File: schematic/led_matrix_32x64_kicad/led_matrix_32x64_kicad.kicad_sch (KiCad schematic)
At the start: 3 parts, among them J1 Conn_02x08_Odd_Even, SW1 SW_Push, U1 Pico

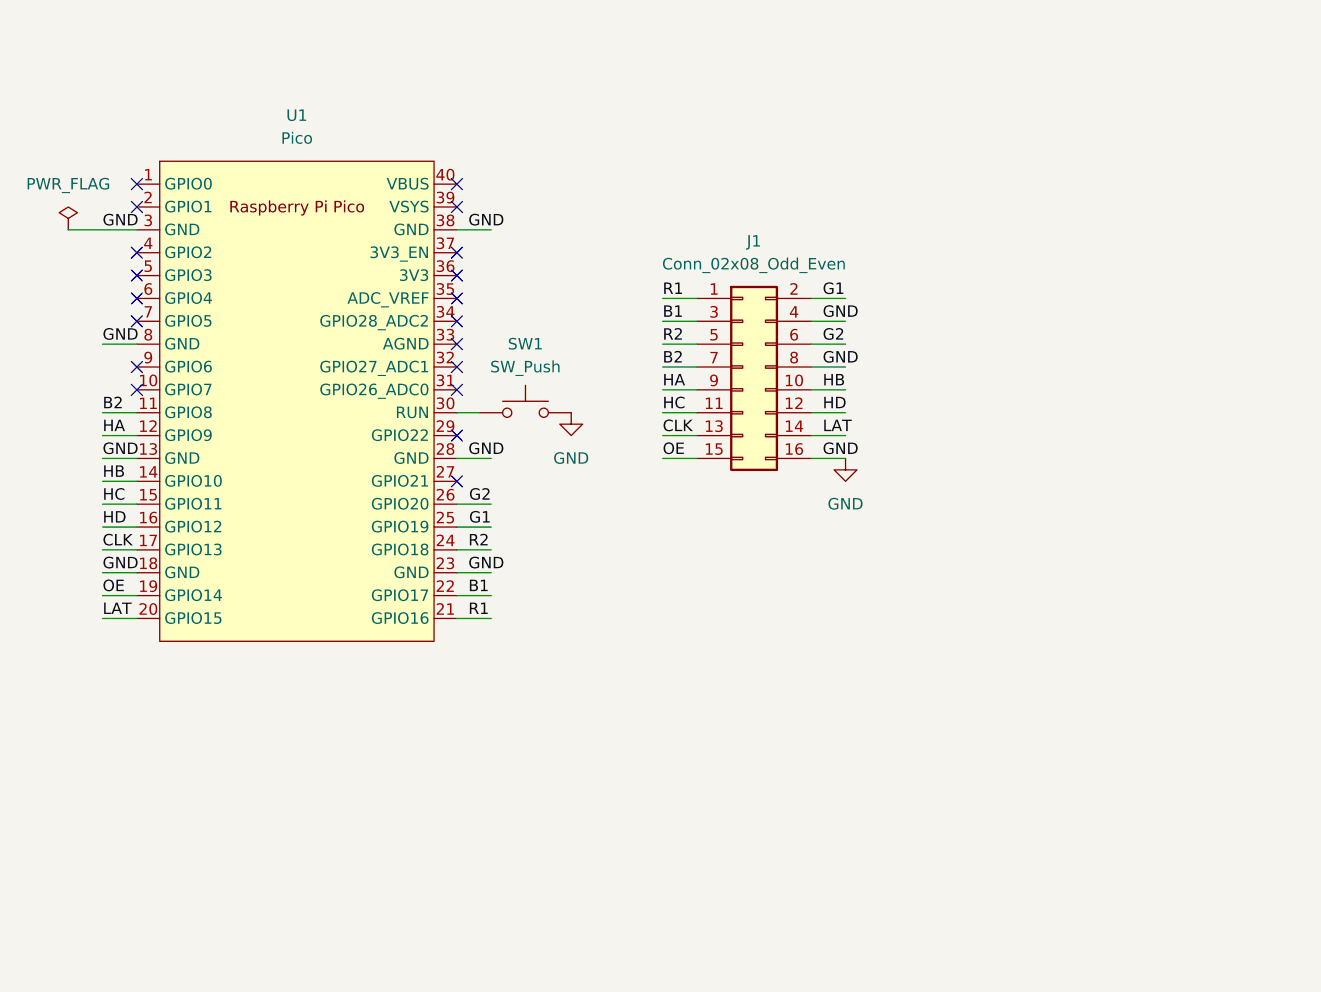
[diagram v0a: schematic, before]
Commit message: Starting the 32x64 matrix with a copy of the 8x8 dotstar.
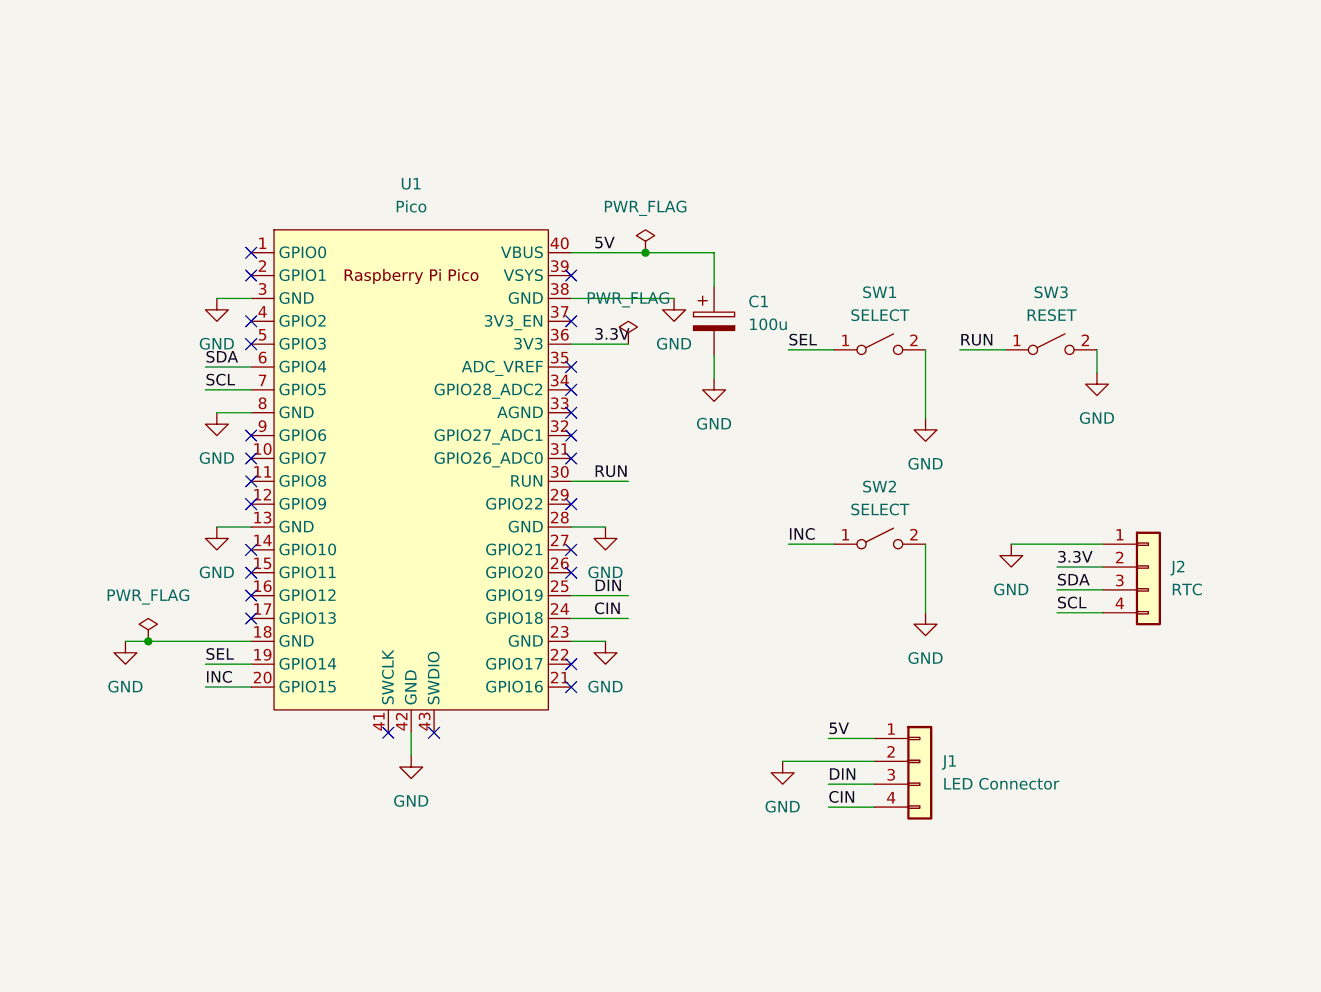
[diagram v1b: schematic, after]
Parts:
- removed J1: Conn_02x08_Odd_Even, Connector_PinHeader_2.54mm:PinHeader_2x08_P2.54mm_Vertical, symbol Connector_Generic:Conn_02x08_Odd_Even
- removed SW1: SW_Push, Button_Switch_THT:SW_PUSH_6mm, symbol Switch:SW_Push
- removed U1: Pico, Raspberry_Pi_Pico:RPi_Pico_SMD_TH, symbol PI PICO:Pico
- added C1: 100u, Capacitor_THT:CP_Radial_D6.3mm_P2.50mm, symbol Device:C_Polarized
- added J1: LED Connector, Connector_PinHeader_2.54mm:PinHeader_1x04_P2.54mm_Vertical, symbol Connector_Generic:Conn_01x04
- added J2: RTC, Connector_PinHeader_2.54mm:PinHeader_1x04_P2.54mm_Vertical, symbol Connector_Generic:Conn_01x04
- added SW1, SW2: SELECT, Button_Switch_THT:SW_PUSH-12mm, symbol Switch:SW_SPST
- added SW3: RESET, Matt:SMD_Button_6mm_3_5mm, symbol Switch:SW_SPST
- added U1: Pico, Raspberry_Pi_Pico:RPi_Pico_SMD_TH, symbol PI Pico:Pico
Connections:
- net GND: now also C1.2, J1.2 (Pin_2), J2.1 (Pin_1), SW1.2 (B), SW2.2 (B), SW3.2 (B), U1.13 (GND), U1.18 (GND), U1.23 (GND), U1.28 (GND), U1.3 (GND), U1.38 (GND), U1.42 (GND), U1.8 (GND)
- new net 3.3V: J2.2 (Pin_2), U1.36 (3V3)
- new net 5V: C1.1, J1.1 (Pin_1), U1.40 (VBUS)
- new net CIN: J1.4 (Pin_4), U1.24 (GPIO18)
- new net DIN: J1.3 (Pin_3), U1.25 (GPIO19)
- new net INC: SW2.1 (A), U1.20 (GPIO15)
- new net RUN: SW3.1 (A), U1.30 (RUN)
- new net SCL: J2.4 (Pin_4), U1.7 (GPIO5)
- new net SDA: J2.3 (Pin_3), U1.6 (GPIO4)
- new net SEL: SW1.1 (A), U1.19 (GPIO14)
- no-connect marks 19 -> 26
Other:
- title: PI Pico to 32x64 LED Matrix interface board -> Matrix Clock

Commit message: Mapped 32x64 pins to PICO
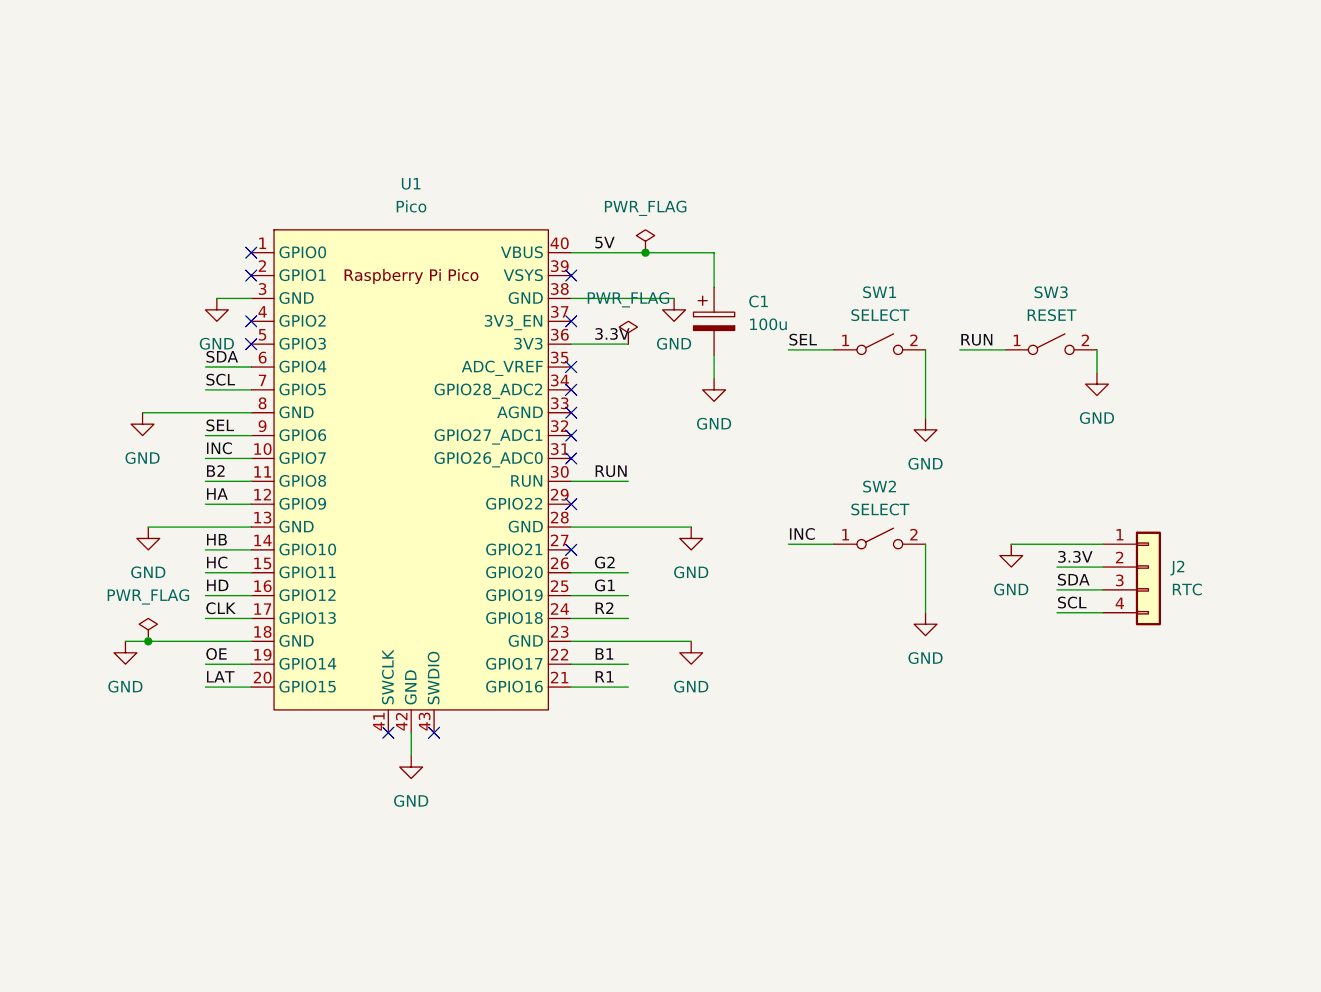
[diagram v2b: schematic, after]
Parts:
- removed J1: LED Connector, Connector_PinHeader_2.54mm:PinHeader_1x04_P2.54mm_Vertical, symbol Connector_Generic:Conn_01x04
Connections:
- net INC: now also U1.10 (GPIO7); no longer U1.20 (GPIO15)
- net SEL: now also U1.9 (GPIO6); no longer U1.19 (GPIO14)
- net B2: now reaches U1.11 (GPIO8)
- net HA: now reaches U1.12 (GPIO9)
- net HB: now reaches U1.14 (GPIO10)
- net HC: now reaches U1.15 (GPIO11)
- net HD: now reaches U1.16 (GPIO12)
- net CLK: now reaches U1.17 (GPIO13)
- net R1: now reaches U1.21 (GPIO16)
- net B1: now reaches U1.22 (GPIO17)
- net G2: now reaches U1.26 (GPIO20)
- net CIN renamed R2
- net DIN renamed G1
- new net LAT: U1.20 (GPIO15)
- new net OE: U1.19 (GPIO14)
- no-connect marks 26 -> 15

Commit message: Updated 32x64 schematic
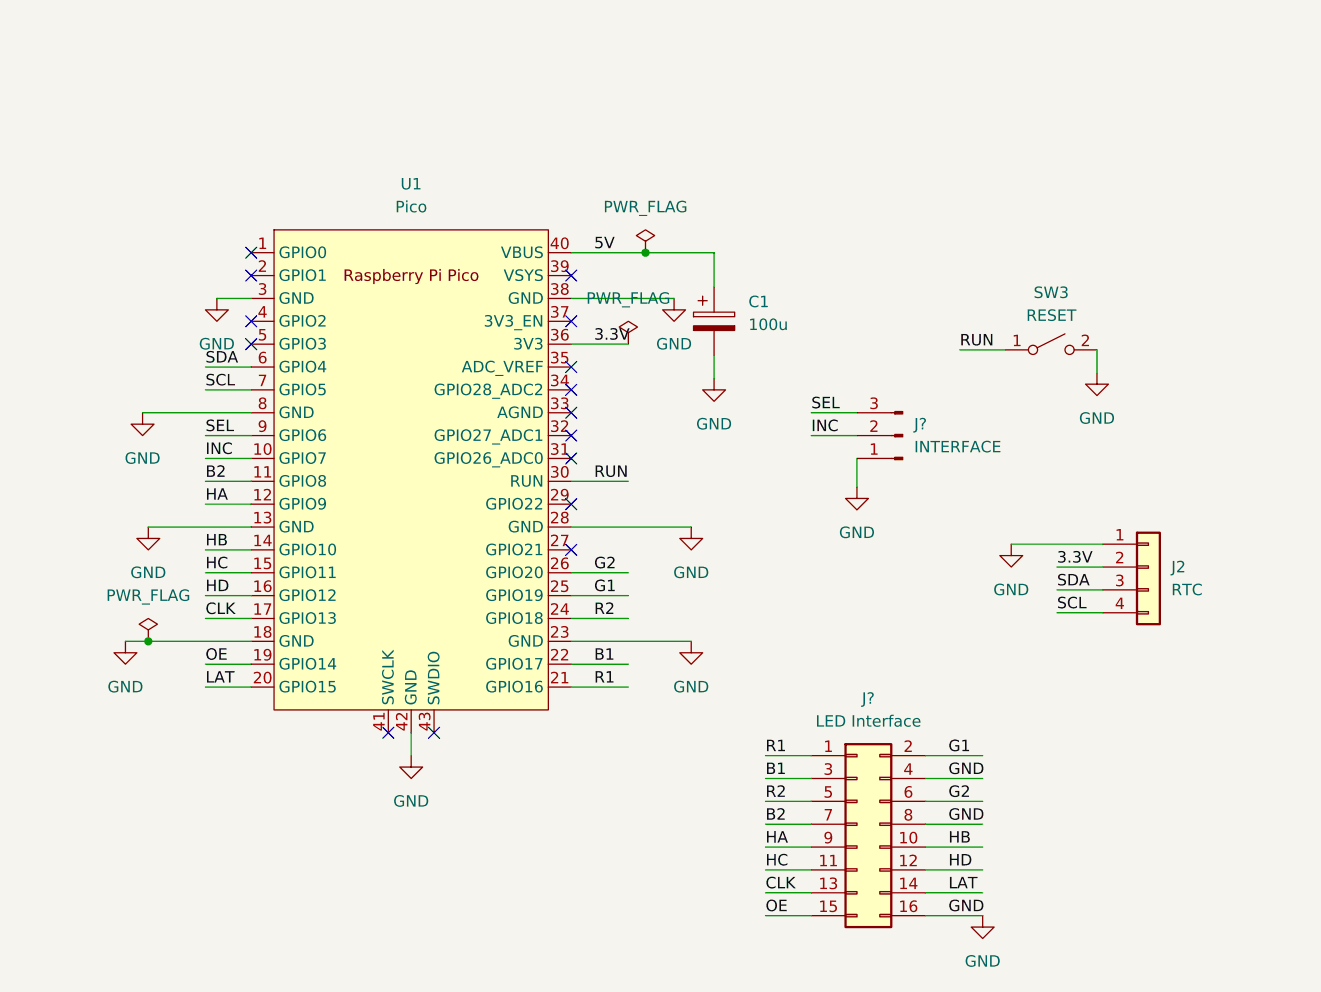
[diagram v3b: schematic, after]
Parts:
- removed SW1, SW2: SELECT, Button_Switch_THT:SW_PUSH-12mm, symbol Switch:SW_SPST
- added J?: LED Interface, Connector_PinHeader_2.54mm:PinHeader_2x08_P2.54mm_Vertical, symbol Connector_Generic:Conn_02x08_Odd_Even
- added J?: INTERFACE, Connector_PinHeader_2.54mm:PinHeader_1x03_P2.54mm_Horizontal, symbol Connector:Conn_01x03_Male
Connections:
- net B1: now also J?.3 (Pin_3)
- net B2: now also J?.7 (Pin_7)
- net CLK: now also J?.13 (Pin_13)
- net G1: now also J?.2 (Pin_2)
- net G2: now also J?.6 (Pin_6)
- net GND: now also J?.1 (Pin_1), J?.16 (Pin_16), J?.4 (Pin_4), J?.8 (Pin_8)
- net HA: now also J?.9 (Pin_9)
- net HB: now also J?.10 (Pin_10)
- net HC: now also J?.11 (Pin_11)
- net HD: now also J?.12 (Pin_12)
- net INC: now also J?.2 (Pin_2)
- net LAT: now also J?.14 (Pin_14)
- net OE: now also J?.15 (Pin_15)
- net R1: now also J?.1 (Pin_1)
- net R2: now also J?.5 (Pin_5)
- net SEL: now also J?.3 (Pin_3)

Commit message: Started on PCB
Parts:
- U1: footprint Raspberry_Pi_Pico:RPi_Pico_SMD_TH -> PI Pico:RPi_Pico_SMD_TH
- gave numbers to parts that had none: 2
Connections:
- net B1: now also J1.4 (Pin_4); no longer J1.3 (Pin_3)
- net B2: now also J1.8 (Pin_8); no longer J1.7 (Pin_7)
- net CLK: now also J1.14 (Pin_14); no longer J1.13 (Pin_13)
- net G1: now also J1.1 (Pin_1); no longer J1.2 (Pin_2)
- net G2: now also J1.5 (Pin_5); no longer J1.6 (Pin_6)
- net GND: now also J1.15 (Pin_15), J1.3 (Pin_3), J1.7 (Pin_7); no longer J1.16 (Pin_16), J1.4 (Pin_4), J1.8 (Pin_8)
- net HA: now also J1.10 (Pin_10); no longer J1.9 (Pin_9)
- net HB: now also J1.9 (Pin_9); no longer J1.10 (Pin_10)
- net HC: now also J1.12 (Pin_12); no longer J1.11 (Pin_11)
- net HD: now also J1.11 (Pin_11); no longer J1.12 (Pin_12)
- net LAT: now also J1.13 (Pin_13); no longer J1.14 (Pin_14)
- net OE: now also J1.16 (Pin_16); no longer J1.15 (Pin_15)
- net R1: now also J1.2 (Pin_2); no longer J1.1 (Pin_1)
- net R2: now also J1.6 (Pin_6); no longer J1.5 (Pin_5)
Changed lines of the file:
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@@
     (effects (font (size 1.27 1.27)) (justify left bottom))
   )
-  (label "HA" (at 149.86 143.51 0)
-    (effects (font (size 1.27 1.27)) (justify left bottom))
-  )
-  (label "GND" (at 170.18 140.97 0)
+  (label "HB" (at 149.86 143.51 0)
+    (effects (font (size 1.27 1.27)) (justify left bottom))
+  )
+  (label "B2" (at 170.18 140.97 0)
     (effects (font (size 1.27 1.27)) (justify left bottom))
   )
@@
     (effects (font (size 1.27 1.27)) (justify left bottom))
   )
-  (label "B2" (at 149.86 140.97 0)
+  (label "GND" (at 149.86 140.97 0)
     (effects (font (size 1.27 1.27)) (justify left bottom))
   )
@@
     (effects (font (size 1.27 1.27)) (justify left bottom))
   )
-  (label "HD" (at 170.18 146.05 0)
-    (effects (font (size 1.27 1.27)) (justify left bottom))
-  )
-  (label "B1" (at 149.86 135.89 0)
-    (effects (font (size 1.27 1.27)) (justify left bottom))
-  )
-  (label "GND" (at 170.18 151.13 0)
-    (effects (font (size 1.27 1.27)) (justify left bottom))
-  )
-  (label "LAT" (at 170.18 148.59 0)
-    (effects (font (size 1.27 1.27)) (justify left bottom))
-  )
-  (label "HB" (at 170.18 143.51 0)
-    (effects (font (size 1.27 1.27)) (justify left bottom))
-  )
-  (label "HC" (at 149.86 146.05 0)
+  (label "HC" (at 170.18 146.05 0)
+    (effects (font (size 1.27 1.27)) (justify left bottom))
+  )
+  (label "GND" (at 149.86 135.89 0)
+    (effects (font (size 1.27 1.27)) (justify left bottom))
+  )
+  (label "OE" (at 170.18 151.13 0)
+    (effects (font (size 1.27 1.27)) (justify left bottom))
+  )
+  (label "CLK" (at 170.18 148.59 0)
+    (effects (font (size 1.27 1.27)) (justify left bottom))
+  )
+  (label "HA" (at 170.18 143.51 0)
+    (effects (font (size 1.27 1.27)) (justify left bottom))
+  )
+  (label "HD" (at 149.86 146.05 0)
     (effects (font (size 1.27 1.27)) (justify left bottom))
   )
@@
     (effects (font (size 1.27 1.27)) (justify left bottom))
   )
-  (label "OE" (at 149.86 151.13 0)
+  (label "GND" (at 149.86 151.13 0)
     (effects (font (size 1.27 1.27)) (justify left bottom))
   )
@@
     (effects (font (size 1.27 1.27)) (justify left bottom))
   )
-  (label "R1" (at 149.86 133.35 0)
+  (label "G1" (at 149.86 133.35 0)
     (effects (font (size 1.27 1.27)) (justify left bottom))
   )
@@
     (effects (font (size 1.27 1.27)) (justify left bottom))
   )
-  (label "CLK" (at 149.86 148.59 0)
+  (label "LAT" (at 149.86 148.59 0)
     (effects (font (size 1.27 1.27)) (justify left bottom))
   )
@@
     (effects (font (size 1.27 1.27)) (justify left bottom))
   )
-  (label "GND" (at 170.18 135.89 0)
-    (effects (font (size 1.27 1.27)) (justify left bottom))
-  )
-  (label "G1" (at 170.18 133.35 0)
-    (effects (font (size 1.27 1.27)) (justify left bottom))
-  )
-  (label "R2" (at 149.86 138.43 0)
-    (effects (font (size 1.27 1.27)) (justify left bottom))
-  )
-  (label "G2" (at 170.18 138.43 0)
+  (label "B1" (at 170.18 135.89 0)
+    (effects (font (size 1.27 1.27)) (justify left bottom))
+  )
+  (label "R1" (at 170.18 133.35 0)
+    (effects (font (size 1.27 1.27)) (justify left bottom))
+  )
+  (label "G2" (at 149.86 138.43 0)
+    (effects (font (size 1.27 1.27)) (justify left bottom))
+  )
+  (label "R2" (at 170.18 138.43 0)
     (effects (font (size 1.27 1.27)) (justify left bottom))
   )
@@
     (pin "1")
   )
-  (symbol (lib_id "power:GND") (at 173.99 151.13 0) (unit 1)
-    (in_bom yes) (on_board yes) (fields_autoplaced)
-    (property "Reference" "#PWR?" (id 0) (at 173.99 157.48 0)
-      (effects (font (size 1.27 1.27)) hide)
-    )
-    (property "Value" "GND" (id 1) (at 173.99 156.21 0))
-    (property "Footprint" "" (id 2) (at 173.99 151.13 0)
-      (effects (font (size 1.27 1.27)) hide)
-    )
-    (property "Datasheet" "" (id 3) (at 173.99 151.13 0)
+  (symbol (lib_id "power:GND") (at 149.86 151.13 0) (unit 1)
+    (in_bom yes) (on_board yes) (fields_autoplaced)
+    (property "Reference" "#PWR07" (id 0) (at 149.86 157.48 0)
+      (effects (font (size 1.27 1.27)) hide)
+    )
+    (property "Value" "GND" (id 1) (at 149.86 156.21 0))
+    (property "Footprint" "" (id 2) (at 149.86 151.13 0)
+      (effects (font (size 1.27 1.27)) hide)
+    )
+    (property "Datasheet" "" (id 3) (at 149.86 151.13 0)
       (effects (font (size 1.27 1.27)) hide)
     )
@@
     (property "Reference" "U1" (id 0) (at 110.49 69.85 0))
     (property "Value" "Pico" (id 1) (at 110.49 72.39 0))
-    (property "Footprint" "Raspberry_Pi_Pico:RPi_Pico_SMD_TH" (id 2) (at 110.49 101.6 90)
+    (property "Footprint" "PI Pico:RPi_Pico_SMD_TH" (id 2) (at 110.49 101.6 90)
       (effects (font (size 1.27 1.27)) hide)
     )
@@
   (symbol (lib_id "Connector_Generic:Conn_02x08_Odd_Even") (at 160.02 140.97 0) (unit 1)
     (in_bom yes) (on_board yes) (fields_autoplaced)
-    (property "Reference" "J?" (id 0) (at 161.29 127 0))
+    (property "Reference" "J1" (id 0) (at 161.29 127 0))
     (property "Value" "LED Interface" (id 1) (at 161.29 129.54 0))
     (property "Footprint" "Connector_PinHeader_2.54mm:PinHeader_2x08_P2.54mm_Vertical" (id 2) (at 160.02 140.97 0)
@@
   (symbol (lib_id "Connector:Conn_01x03_Male") (at 165.1 97.79 180) (unit 1)
     (in_bom yes) (on_board yes) (fields_autoplaced)
-    (property "Reference" "J?" (id 0) (at 166.37 96.5199 0)
+    (property "Reference" "J3" (id 0) (at 166.37 96.5199 0)
       (effects (font (size 1.27 1.27)) (justify right))
     )
@@
       (reference "#PWR06") (unit 1) (value "GND") (footprint "")
     )
+    (path "/439ec49a-2dfb-4044-a14b-923720000ce6"
+      (reference "#PWR07") (unit 1) (value "GND") (footprint "")
+    )
     (path "/6396dcee-0336-47ed-a795-08acc98eb796"
       (reference "#PWR08") (unit 1) (value "GND") (footprint "")
@@
       (reference "#PWR016") (unit 1) (value "GND") (footprint "")
     )
-    (path "/439ec49a-2dfb-4044-a14b-923720000ce6"
-      (reference "#PWR?") (unit 1) (value "GND") (footprint "")
-    )
     (path "/87e5dc14-ec2c-4db9-b820-3bcc7c160b8a"
       (reference "C1") (unit 1) (value "100u") (footprint "Capacitor_THT:CP_Radial_D6.3mm_P2.50mm")
     )
+    (path "/b44020fe-f3bb-4f9c-a831-737f7e5c7489"
+      (reference "J1") (unit 1) (value "LED Interface") (footprint "Connector_PinHeader_2.54mm:PinHeader_2x08_P2.54mm_Vertical")
+    )
     (path "/0620a211-528d-48eb-9a45-21dab6b26f64"
       (reference "J2") (unit 1) (value "RTC") (footprint "Connector_PinHeader_2.54mm:PinHeader_1x04_P2.54mm_Vertical")
     )
-    (path "/b44020fe-f3bb-4f9c-a831-737f7e5c7489"
-      (reference "J?") (unit 1) (value "LED Interface") (footprint "Connector_PinHeader_2.54mm:PinHeader_2x08_P2.54mm_Vertical")
-    )
     (path "/e4551e8b-ee53-4dd9-856d-2c35a094085d"
-      (reference "J?") (unit 1) (value "INTERFACE") (footprint "Connector_PinHeader_2.54mm:PinHeader_1x03_P2.54mm_Horizontal")
+      (reference "J3") (unit 1) (value "INTERFACE") (footprint "Connector_PinHeader_2.54mm:PinHeader_1x03_P2.54mm_Horizontal")
     )
     (path "/f91c723a-0bca-4356-9537-04c9b611b4f3"
@@
     )
     (path "/588e08bc-80dd-4d59-ac18-24f0d8657078"
-      (reference "U1") (unit 1) (value "Pico") (footprint "Raspberry_Pi_Pico:RPi_Pico_SMD_TH")
-    )
-  )
+      (reference "U1") (unit 1) (value "Pico") (footprint "PI Pico:RPi_Pico_SMD_TH")
+    )
+  )
